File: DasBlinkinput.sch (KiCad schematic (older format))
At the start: 9 parts, among them P101 CONN_01X02, P102 CONN_01X01, P103 CONN_01X01, P104 CONN_01X05, U101 LP2980

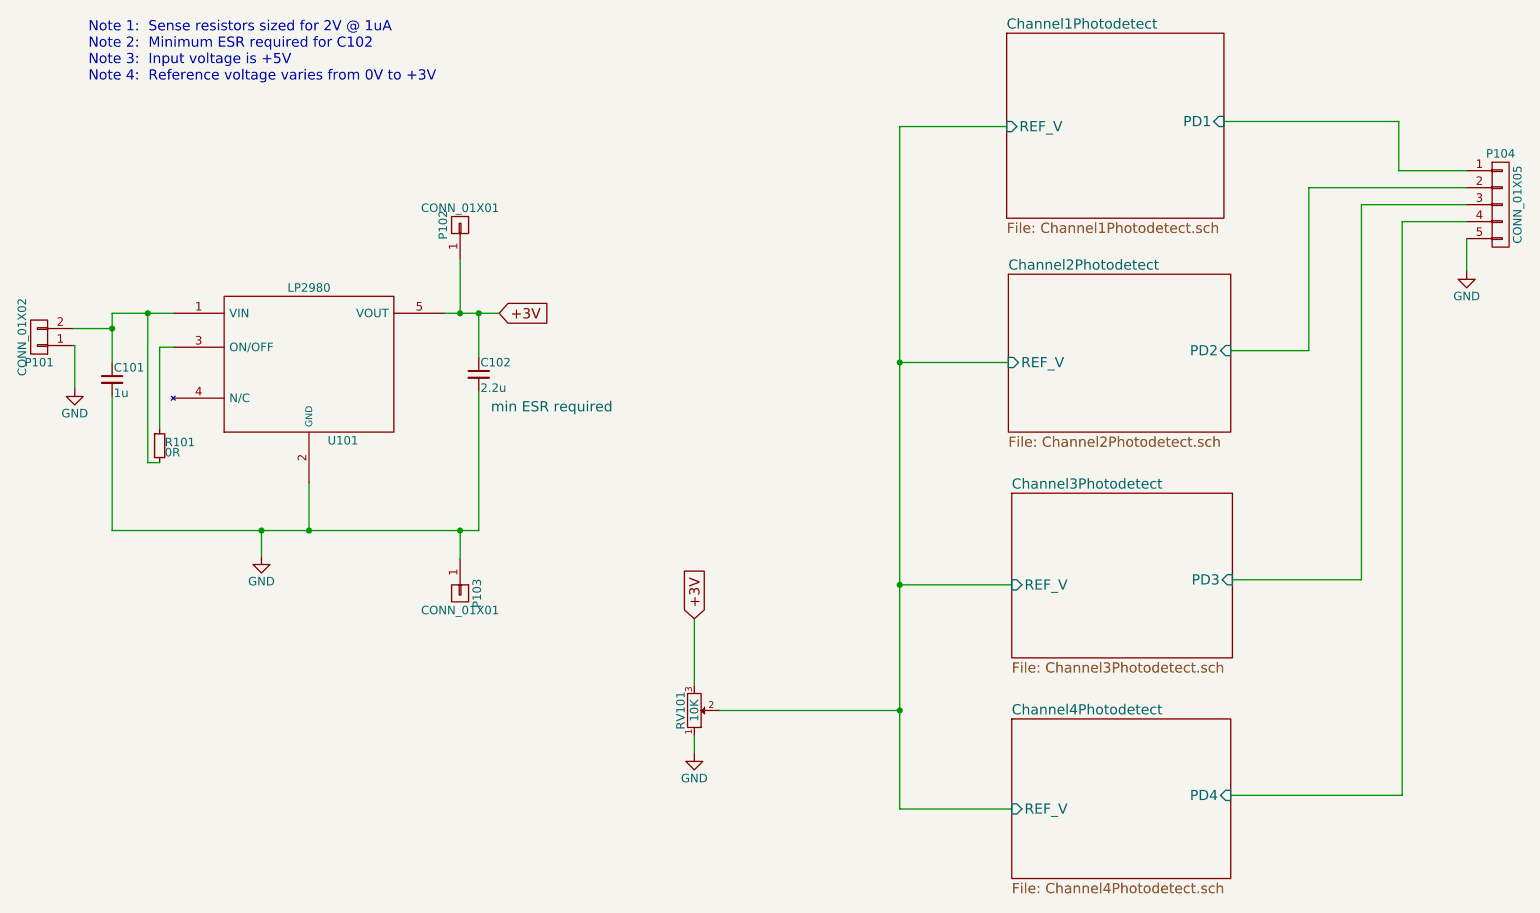
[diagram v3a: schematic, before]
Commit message: completed pcb basic layout
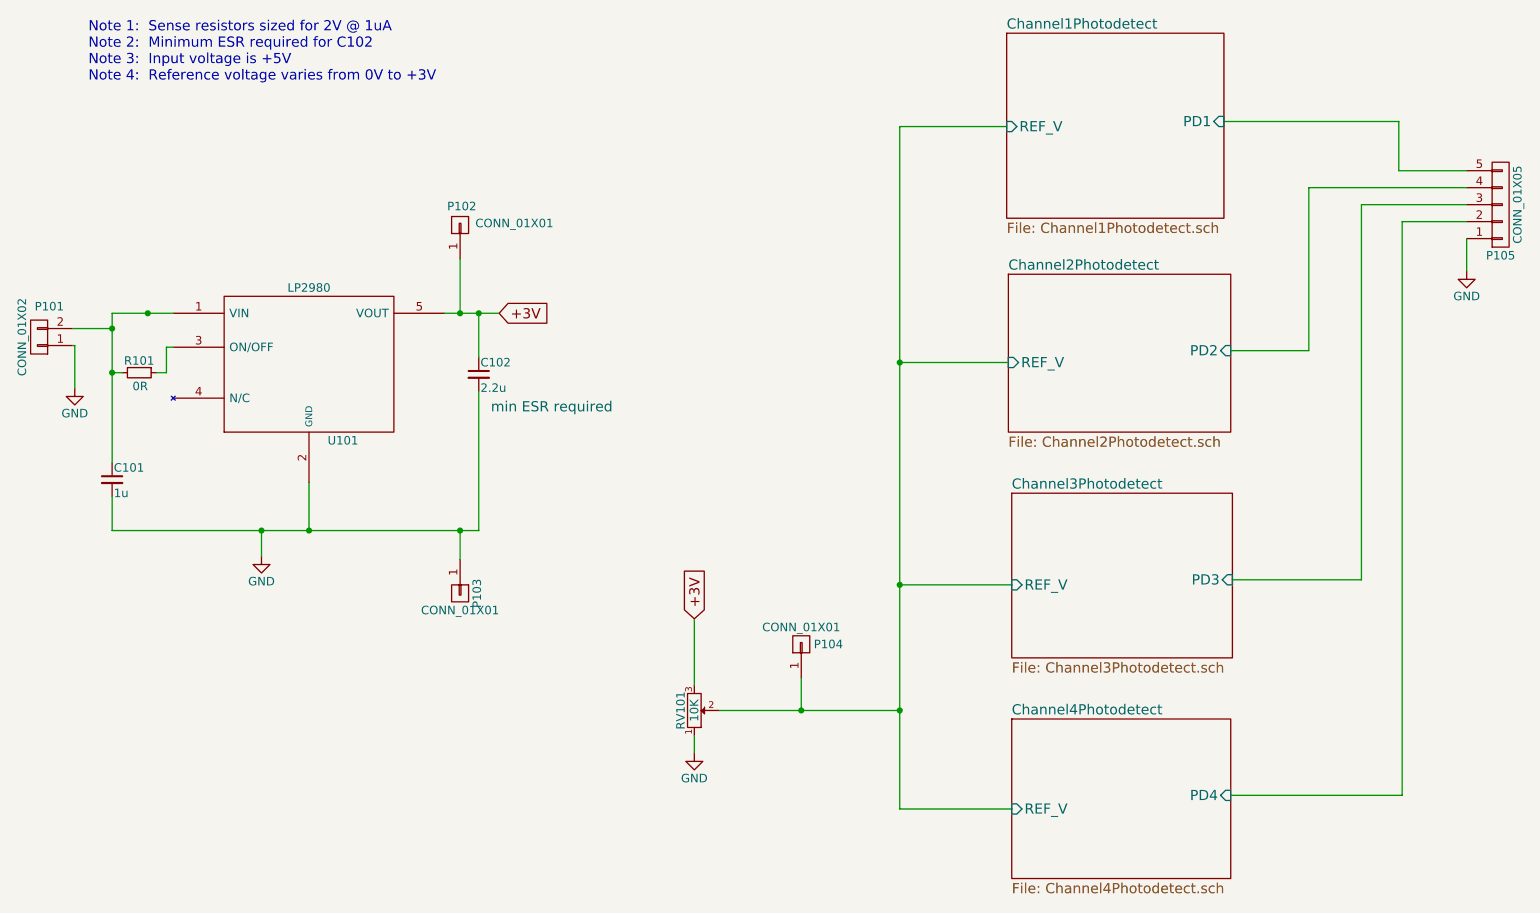
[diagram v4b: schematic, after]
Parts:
- added P104: CONN_01X01, Pin_Headers:Pin_Header_Straight_1x01, symbol CONN_01X01
- renumbered P104 to P105
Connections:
- net Channel1Photodetect/PD1: now also P105.5 (P5); no longer P105.1 (P1)
- net Channel1Photodetect/REF_V: now also P104.1 (P1)
- net Channel2Photodetect/PD2: now also P105.4 (P4); no longer P105.2 (P2)
- net Channel4Photodetect/PD4: now also P105.2 (P2); no longer P105.4 (P4)
- net GND: now also P105.1 (P1); no longer P105.5 (P5)
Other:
- moved on the sheet: C101, R101
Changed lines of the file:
@@
 $EndComp
 $Comp
-L GND #PWR01
+L GND #PWR102
 U 1 1 5823699E
 P 2070 3870
-F 0 "#PWR01" H 2070 3620 50  0001 C CNN
+F 0 "#PWR102" H 2070 3620 50  0001 C CNN
 F 1 "GND" H 2070 3720 50  0000 C CNN
 F 2 "" H 2070 3870 50  0000 C CNN
@@
 L R_Small R101
 U 1 1 582369B4
-P 1470 3220
-F 0 "R101" H 1500 3240 50  0000 L CNN
-F 1 "0R" H 1500 3180 50  0000 L CNN
-F 2 "Resistors_SMD:R_0805_HandSoldering" H 1470 3220 50  0001 C CNN
-F 3 "" H 1470 3220 50  0000 C CNN
-F 4 "Value" H 1470 3220 60  0001 C CNN "Fieldname"
-	1    1470 3220
-	1    0    0    -1
+P 1350 2790
+F 0 "R101" V 1280 2700 50  0000 L CNN
+F 1 "0R" V 1430 2750 50  0000 L CNN
+F 2 "Resistors_SMD:R_0805_HandSoldering" H 1350 2790 50  0001 C CNN
+F 3 "" H 1350 2790 50  0000 C CNN
+F 4 "Value" H 1350 2790 60  0001 C CNN "Fieldname"
+	1    1350 2790
+	0    1    1    0
 $EndComp
 $Comp
 L C_Small C101
 U 1 1 58236A11
-P 1190 2830
-F 0 "C101" H 1200 2900 50  0000 L CNN
-F 1 "1u" H 1200 2750 50  0000 L CNN
-F 2 "Capacitors_SMD:C_0805_HandSoldering" H 1190 2830 50  0001 C CNN
-F 3 "" H 1190 2830 50  0000 C CNN
-F 4 "Value" H 1190 2830 60  0001 C CNN "Fieldname"
-	1    1190 2830
+P 1190 3420
+F 0 "C101" H 1200 3490 50  0000 L CNN
+F 1 "1u" H 1200 3340 50  0000 L CNN
+F 2 "Capacitors_SMD:C_0805_HandSoldering" H 1190 3420 50  0001 C CNN
+F 3 "" H 1190 3420 50  0000 C CNN
+F 4 "Value" H 1190 3420 60  0001 C CNN "Fieldname"
+	1    1190 3420
 	1    0    0    -1
 $EndComp
@@
 U 1 1 58237082
 P 3240 1920
-F 0 "P102" H 3240 2020 50  0000 C CNN
-F 1 "CONN_01X01" V 3340 1920 50  0000 C CNN
+F 0 "P102" V 3350 1910 50  0000 C CNN
+F 1 "CONN_01X01" V 3250 1600 50  0000 C CNN
 F 2 "Pin_Headers:Pin_Header_Straight_1x01" H 3240 1920 50  0001 C CNN
 F 3 "" H 3240 1920 50  0000 C CNN
@@
 U 1 1 582370EA
 P 760 2580
-F 0 "P101" H 760 2730 50  0000 C CNN
+F 0 "P101" H 700 2400 50  0000 C CNN
 F 1 "CONN_01X02" V 860 2580 50  0000 C CNN
 F 2 "Pin_Headers:Pin_Header_Straight_1x02" H 760 2580 50  0001 C CNN
@@
 $EndComp
 $Comp
-L GND #PWR02
+L GND #PWR101
 U 1 1 58237150
 P 970 2880
-F 0 "#PWR02" H 970 2630 50  0001 C CNN
+F 0 "#PWR101" H 970 2630 50  0001 C CNN
 F 1 "GND" H 970 2730 50  0000 C CNN
 F 2 "" H 970 2880 50  0000 C CNN
@@
 $EndComp
 $Comp
-L GND #PWR03
+L GND #PWR103
 U 1 1 582376FF
 P 4620 5030
-F 0 "#PWR03" H 4620 4780 50  0001 C CNN
+F 0 "#PWR103" H 4620 4780 50  0001 C CNN
 F 1 "GND" H 4620 4880 50  0000 C CNN
 F 2 "" H 4620 5030 50  0000 C CNN
@@
 	1    0    0    -1
 $EndComp
-Wire Wire Line
-	2350 3720 2350 3440
-Wire Wire Line
-	1190 3720 3350 3720
-Wire Wire Line
-	1190 3720 1190 2930
-Wire Wire Line
-	1470 3120 1470 2640
-Wire Wire Line
-	1470 2640 1550 2640
-Wire Wire Line
-	1190 2440 1550 2440
-Wire Wire Line
-	1190 2440 1190 2730
-Wire Wire Line
-	3150 2440 3470 2440
-Wire Wire Line
-	3350 2440 3350 2700
-Wire Wire Line
-	3350 3720 3350 2900
-Connection ~ 2350 3720
-Connection ~ 3350 2440
-Wire Wire Line
-	3240 2120 3240 2440
-Connection ~ 3240 2440
-Wire Wire Line
-	3240 3890 3240 3720
-Connection ~ 3240 3720
-Wire Wire Line
-	960  2530 1190 2530
-Connection ~ 1190 2530
-Wire Wire Line
-	960  2630 970  2630
-Wire Wire Line
-	970  2630 970  2880
-Wire Wire Line
-	5830 1340 6460 1340
-Wire Wire Line
-	6470 2730 5830 2730
-Wire Wire Line
-	5830 4040 6490 4040
-Wire Wire Line
-	5830 5360 6490 5360
-$Comp
-L CONN_01X05 P104
+$Comp
+L CONN_01X05 P105
 U 1 1 5823B1B0
 P 9370 1800
-F 0 "P104" H 9370 2100 50  0000 C CNN
+F 0 "P105" H 9370 2100 50  0000 C CNN
 F 1 "CONN_01X05" V 9470 1800 50  0000 C CNN
 F 2 "Pin_Headers:Pin_Header_Straight_1x05" H 9370 1800 50  0001 C CNN
 F 3 "" H 9370 1800 50  0000 C CNN
 	1    9370 1800
-	1    0    0    -1
-$EndComp
-Wire Wire Line
-	7740 1310 8770 1310
-Wire Wire Line
-	8770 1310 8770 1600
-Wire Wire Line
-	8770 1600 9170 1600
-Wire Wire Line
-	7780 2660 8240 2660
-Wire Wire Line
-	8240 2660 8240 1700
-Wire Wire Line
-	8240 1700 9170 1700
-Wire Wire Line
-	7790 4010 8550 4010
-Wire Wire Line
-	8550 4010 8550 1800
-Wire Wire Line
-	8550 1800 9170 1800
-Wire Wire Line
-	7780 5280 8790 5280
-Wire Wire Line
-	8790 5280 8790 1900
-Wire Wire Line
-	8790 1900 9170 1900
-$Comp
-L GND #PWR04
+	1    0    0    1
+$EndComp
+$Comp
+L GND #PWR104
 U 1 1 5823BAF8
 P 9170 2190
-F 0 "#PWR04" H 9170 1940 50  0001 C CNN
+F 0 "#PWR104" H 9170 1940 50  0001 C CNN
 F 1 "GND" H 9170 2040 50  0000 C CNN
 F 2 "" H 9170 2190 50  0000 C CNN
@@
 	1    0    0    -1
 $EndComp
+Text Notes 1050 1080 0    60   ~ 0
+Note 1:  Sense resistors sized for 2V @ 1uA\nNote 2:  Minimum ESR required for C102\nNote 3:  Input voltage is +5V\nNote 4:  Reference voltage varies from 0V to +3V
+$Comp
+L CONN_01X01 P104
+U 1 1 58378D35
+P 5250 4390
+F 0 "P104" V 5250 4230 50  0000 C CNN
+F 1 "CONN_01X01" V 5350 4390 50  0000 C CNN
+F 2 "Pin_Headers:Pin_Header_Straight_1x01" H 5250 4390 50  0001 C CNN
+F 3 "" H 5250 4390 50  0000 C CNN
+F 4 "Value" H 5250 4390 60  0001 C CNN "Fieldname"
+F 5 "VREF" H 5250 4390 60  0001 C CNN "Label"
+	1    5250 4390
+	0    -1   -1   0
+$EndComp
+Wire Wire Line
+	2350 3720 2350 3440
+Wire Wire Line
+	1190 3720 3350 3720
+Wire Wire Line
+	1190 3720 1190 3520
+Wire Wire Line
+	1190 2440 1550 2440
+Wire Wire Line
+	1190 2440 1190 3320
+Wire Wire Line
+	3150 2440 3470 2440
+Wire Wire Line
+	3350 2440 3350 2700
+Wire Wire Line
+	3350 3720 3350 2900
+Connection ~ 2350 3720
+Connection ~ 3350 2440
+Wire Wire Line
+	3240 2120 3240 2440
+Connection ~ 3240 2440
+Wire Wire Line
+	3240 3890 3240 3720
+Connection ~ 3240 3720
+Wire Wire Line
+	960  2530 1190 2530
+Connection ~ 1190 2530
+Wire Wire Line
+	960  2630 970  2630
+Wire Wire Line
+	970  2630 970  2880
+Wire Wire Line
+	5830 1340 6460 1340
+Wire Wire Line
+	6470 2730 5830 2730
+Wire Wire Line
+	5830 4040 6490 4040
+Wire Wire Line
+	5830 5360 6490 5360
+Wire Wire Line
+	7740 1310 8770 1310
+Wire Wire Line
+	8770 1310 8770 1600
+Wire Wire Line
+	7780 2660 8240 2660
+Wire Wire Line
+	8240 2660 8240 1700
+Wire Wire Line
+	8240 1700 9170 1700
+Wire Wire Line
+	7790 4010 8550 4010
+Wire Wire Line
+	8550 4010 8550 1800
+Wire Wire Line
+	8550 1800 9170 1800
+Wire Wire Line
+	7780 5280 8790 5280
+Wire Wire Line
+	8790 5280 8790 1900
+Wire Wire Line
+	8790 1900 9170 1900
 Wire Wire Line
 	9170 2000 9170 2190
@@
 	2070 3870 2070 3720
 Connection ~ 2070 3720
-Text Notes 1050 1080 0    60   ~ 0
-Note 1:  Sense resistors sized for 2V @ 1uA\nNote 2:  Minimum ESR required for C102\nNote 3:  Input voltage is +5V\nNote 4:  Reference voltage varies from 0V to +3V
 Wire Wire Line
 	5830 1340 5830 5360
@@
 Wire Wire Line
 	4620 4240 4620 4630
-Wire Wire Line
-	1400 3320 1470 3320
-Wire Wire Line
-	1400 3320 1400 2440
 Connection ~ 1400 2440
+Wire Wire Line
+	1250 2790 1190 2790
+Connection ~ 1190 2790
+Wire Wire Line
+	1550 2640 1510 2640
+Wire Wire Line
+	1510 2640 1510 2790
+Wire Wire Line
+	1510 2790 1450 2790
+Wire Wire Line
+	5250 4590 5250 4780
+Connection ~ 5250 4780
+Wire Wire Line
+	8770 1600 9170 1600
 $EndSCHEMATC

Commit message: udated notes on schematic
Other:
- note added: "Note 1: Sense resistors sized for 2V @ 2uA\nNote 2: Minimum ESR required for C102\nNote 3: Input voltage is +5V\nNote 4: Reference voltage varies from 0V to +3V"
- note removed: "Note 1: Sense resistors sized for 2V @ 1uA\nNote 2: Minimum ESR required for C102\nNote 3: Input voltage is +5V\nNote 4: Reference voltage varies from 0V to +3V"
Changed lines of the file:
@@
 $EndComp
 Text Notes 1050 1080 0    60   ~ 0
-Note 1:  Sense resistors sized for 2V @ 1uA\nNote 2:  Minimum ESR required for C102\nNote 3:  Input voltage is +5V\nNote 4:  Reference voltage varies from 0V to +3V
+Note 1:  Sense resistors sized for 2V @ 2uA\nNote 2:  Minimum ESR required for C102\nNote 3:  Input voltage is +5V\nNote 4:  Reference voltage varies from 0V to +3V
 $Comp
 L CONN_01X01 P104

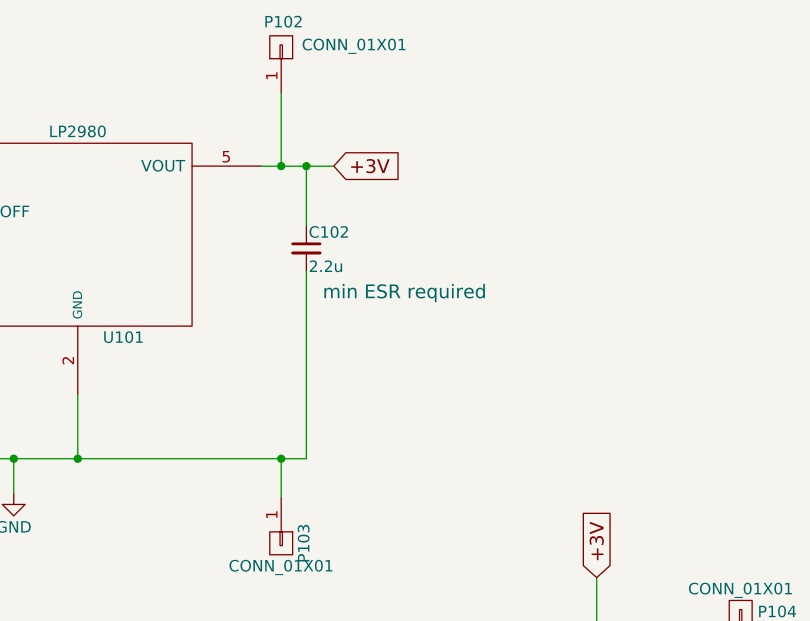
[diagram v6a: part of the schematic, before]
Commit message: changed tantalum cap to polarized symbol and tantalum footprint
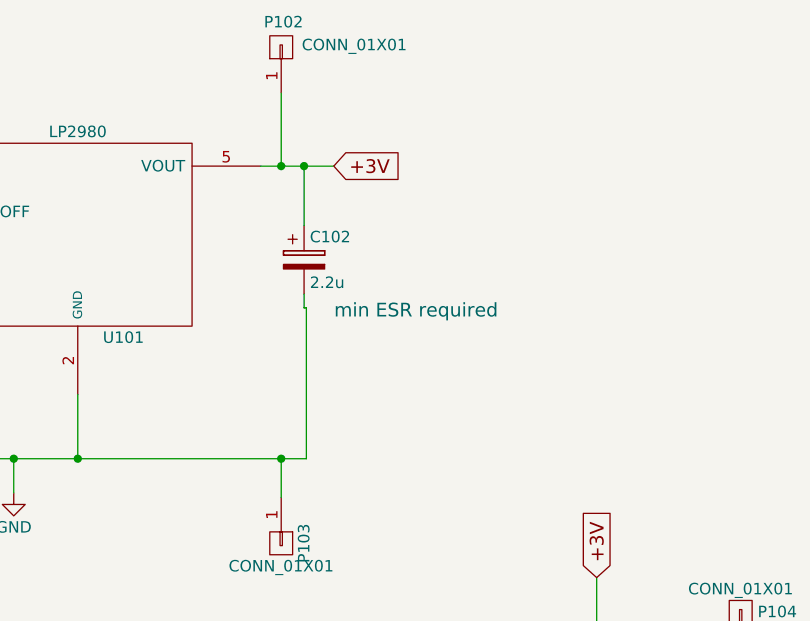
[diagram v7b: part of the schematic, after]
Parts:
- removed C102: 2.2u, Capacitors_SMD:C_1206_HandSoldering, symbol C_Small
- added C102: 2.2u, Capacitors_Tantalum_SMD:TantalC_SizeA_EIA-3216_HandSoldering, symbol CP
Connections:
- net +3V: now also C102.1
- net GND: now also C102.2
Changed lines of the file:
@@
-	1    0    0    -1
-$EndComp
-$Comp
-L C_Small C102
-U 1 1 58236A51
-P 3350 2800
-F 0 "C102" H 3360 2870 50  0000 L CNN
-F 1 "2.2u" H 3360 2720 50  0000 L CNN
-F 2 "Capacitors_SMD:C_1206_HandSoldering" H 3350 2800 50  0001 C CNN
-F 3 "http://www.vishay.com/docs/40002/293d.pdf" H 3350 2800 50  0001 C CNN
-F 4 "Value" H 3350 2800 60  0001 C CNN "Fieldname"
-F 5 "293D225X0010A2TE3" H 3350 2800 60  0001 C CNN "MPN"
-F 6 "min ESR required" H 3780 2610 60  0000 C CNN "Note"
-	1    3350 2800
 	1    0    0    -1
 $EndComp
@@
 Wire Wire Line
 	3150 2440 3470 2440
-Wire Wire Line
-	3350 2440 3350 2700
-Wire Wire Line
-	3350 3720 3350 2900
 Connection ~ 2350 3720
-Connection ~ 3350 2440
 Wire Wire Line
 	3240 2120 3240 2440
@@
 Wire Wire Line
 	8770 1600 9170 1600
+$Comp
+L CP C102
+U 1 1 588404ED
+P 3340 2850
+F 0 "C102" H 3365 2950 50  0000 L CNN
+F 1 "2.2u" H 3365 2750 50  0000 L CNN
+F 2 "Capacitors_Tantalum_SMD:TantalC_SizeA_EIA-3216_HandSoldering" H 3378 2700 50  0001 C CNN
+F 3 "http://www.vishay.com/docs/40002/293d.pdf" H 3340 2850 50  0001 C CNN
+F 4 "Value" H 3340 2850 60  0001 C CNN "Fieldname"
+F 5 "293D225X0010A2TE3" H 3340 2850 60  0001 C CNN "MPN"
+F 6 "min ESR required" H 3830 2630 60  0000 C CNN "Note"
+	1    3340 2850
+	1    0    0    -1
+$EndComp
+Wire Wire Line
+	3340 2700 3340 2440
+Connection ~ 3340 2440
+Wire Wire Line
+	3350 3720 3350 3060
+Wire Wire Line
+	3350 3060 3340 3060
+Wire Wire Line
+	3340 3060 3340 3000
 $EndSCHEMATC
